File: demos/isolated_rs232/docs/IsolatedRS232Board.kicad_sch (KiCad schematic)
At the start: 9 parts, among them J1 Header1xNFemale, J2 Header1xNFemale

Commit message: export: kicad_sch — Phase 2.5b: layered placement, wire routing, KiCad 10 compatibility (#23)
* export: kicad_sch — Phase 2.5b: layered placement + routing + KiCad 9 fix

Placement (placement.py, complete rewrite):
- Replaces naive grid with Layered Signal Flow algorithm (spec §5 stages 1–8)
- Stage 1: band classification — power chips/rails at top, LEDs at bottom,
  everything else in the signal band
- Stage 2: signal-flow DAG via BFS from Rail/Connector sources; layer = BFS
  distance from nearest source
- Stage 3–4: place within (band, layer) cells at 1500-mil (38.1 mm) same-band
  spacing, 1000-mil inter-band gutter, 25.4 mm page margin
- Stage 6: cluster breakup — up to 10 iterations shifting same-band parts
  that land closer than 0.9× SAME_BAND_SPACING_MM
- Stage 8: page sized to fit (A4 → A3 → A2 → A1)
- grid_place() and sheet_size_mm() kept as shims for backward-compat

Routing (routing.py, new file):
- route_net(): connects stub ends with Manhattan L-shapes (horizontal first)
- find_junctions(): returns points where ≥3 wire endpoints coincide
- renderer uses routed wires between signal-net stub ends

Hierarchical (hierarchical.py, new file):
- collect_boards(), is_multi_board(), sub_sheet_filename() — interface stub
  for multi-Board sub-sheet emission (full implementation deferred)

KiCad 9 sub-symbol name fix (library_loader.py):
- KiCad 9 schematics expect sub-symbols nested inside their parent in
  lib_symbols to use the bare name (R_0_1, LED_0_1, 4069_1_0) — NOT the
  lib-qualified name (Device:R_0_1, Device:LED_0_1, 4xxx:4069_1_0)
- Fixed _qualify_names() to add the lib: prefix only to the exact parent
  symbol name using a lookahead (?=") that prevents sub-unit names from
  being qualified

Tests (+25 tests):
- test_placement.py: band classification, all-on-grid, determinism,
  minimum spacing, power < signal < indicator Y ordering, page sizing
- test_routing.py: H/V segments, L-shapes, orthogonality, grid snap,
  junction detection

Golden files re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
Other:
- moved on the sheet: C1, C2, C3, C4, C5, C6, C7, J1, J2

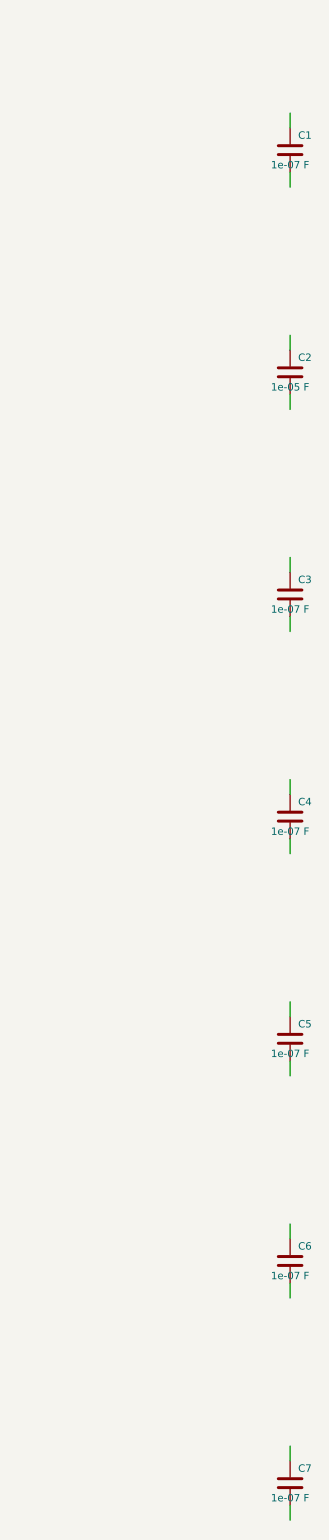
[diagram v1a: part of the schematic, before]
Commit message: framework: passive + diode terminals mandatory (#30)
Continuation of the LED.cathode regression fix (#29). Resistor,
Capacitor, Inductor, and every Diode subclass had their terminals
declared `mandatory=False` with the same "structurally inert under
graph evaluation" justification — letting demos declare BOM-only
timing / decoupling / pull-up parts without wiring them, then ship
breadboard SVGs and netlists where those parts sat orphaned.

A real resistor / capacitor / inductor / diode with a dangling
terminal does nothing. Marking the ports mandatory closes the
silent regression at the framework layer.

  - `src/components/passives/{resistor,capacitor,inductor}.py` and
    every diode subclass under `src/components/diodes/` now declare
    their terminals `mandatory=True`.
  - `tests/components/test_{resistor,capacitor,inductor}.py`:
    regression tests pin the new contract per component.
  - `tests/components/test_diode_mandatory_terminals.py` (new):
    parametrized over D1N4001 / D1N4007 / D1N4148 / D1N4728A /
    D1N4733A / D1N4742A / D1N5817.
  - Six demos (`backup_power`, `bldc_motor`, `dice`,
    `doorbell_protector`, `fan_cooling`, `isolated_rs232`) had
    declared-but-unwired passives — each now wires them either to
    their datasheet-correct net (e.g. DoorbellProtector's flyback
    diode anode joins the relay coil_minus net) or as an isolated
    0-Ω passthrough with `dynamically_driven=True` where the part
    is genuinely BOM-only and the voltage-only simulator can't
    honour its behaviour. Comments at each call site explain
    which kind.
  - Test fixtures across CLI, refdes, format-roundtrip, kicad
    import, and per-format renderer tests updated so they still
    pin down the specific error each one exists to catch without
    tripping the new mandatory-pin check first.
  - All demo docs regenerated; goldens refreshed.

After this commit the breadboard SVGs show every BOM part connected
to something — no more orphaned caps and resistors float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
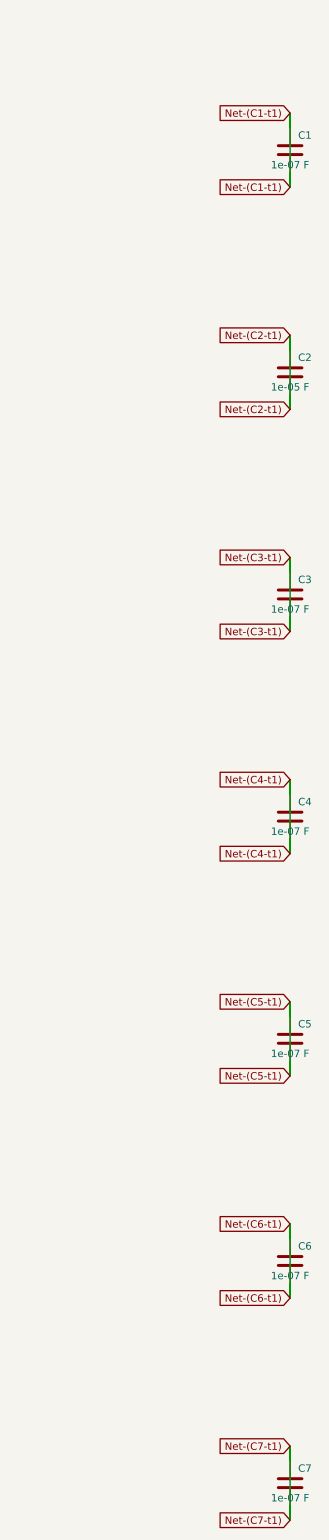
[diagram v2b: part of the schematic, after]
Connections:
- net Net-(C2-t1): now reaches C2.1
- net Net-(C2-t1): now also C2.2
- net Net-(C7-t1): now reaches C7.1
- net Net-(C7-t1): now also C7.2
- net Net-(C3-t1): now reaches C3.1
- net Net-(C3-t1): now also C3.2
- net Net-(C4-t1): now reaches C4.1
- net Net-(C4-t1): now also C4.2
- net Net-(C1-t1): now reaches C1.1
- net Net-(C1-t1): now also C1.2
- net Net-(C5-t1): now reaches C5.1
- net Net-(C5-t1): now also C5.2
- net Net-(C6-t1): now reaches C6.1
- net Net-(C6-t1): now also C6.2
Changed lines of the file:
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@@
     (stroke (width 0) (type default))
+  )
+  (global_label "Net-(C1-t1)"
+    (shape input)
+    (at 63.5 184.15 0)
+    (fields_autoplaced yes)
+    (effects (font (size 1.27 1.27)) (justify right))
+    (property "Intersheet References" "${INTERSHEET_REFS}"
+      (at 0 0 0)
+      (effects (font (size 1.27 1.27)) (hide yes))
+    )
   )
   (wire
     (pts (xy 63.5 173.99) (xy 63.5 171.45))
     (stroke (width 0) (type default))
+  )
+  (global_label "Net-(C1-t1)"
+    (shape input)
+    (at 63.5 171.45 0)
+    (fields_autoplaced yes)
+    (effects (font (size 1.27 1.27)) (justify right))
+    (property "Intersheet References" "${INTERSHEET_REFS}"
+      (at 0 0 0)
+      (effects (font (size 1.27 1.27)) (hide yes))
+    )
   )
   (symbol
@@
     (stroke (width 0) (type default))
   )
+  (global_label "Net-(C2-t1)"
+    (shape input)
+    (at 63.5 222.25 0)
+    (fields_autoplaced yes)
+    (effects (font (size 1.27 1.27)) (justify right))
+    (property "Intersheet References" "${INTERSHEET_REFS}"
+      (at 0 0 0)
+      (effects (font (size 1.27 1.27)) (hide yes))
+    )
+  )
   (wire
     (pts (xy 63.5 212.09) (xy 63.5 209.55))
     (stroke (width 0) (type default))
+  )
+  (global_label "Net-(C2-t1)"
+    (shape input)
+    (at 63.5 209.55 0)
+    (fields_autoplaced yes)
+    (effects (font (size 1.27 1.27)) (justify right))
+    (property "Intersheet References" "${INTERSHEET_REFS}"
+      (at 0 0 0)
+      (effects (font (size 1.27 1.27)) (hide yes))
+    )
   )
   (symbol
@@
     (stroke (width 0) (type default))
   )
+  (global_label "Net-(C3-t1)"
+    (shape input)
+    (at 63.5 260.35 0)
+    (fields_autoplaced yes)
+    (effects (font (size 1.27 1.27)) (justify right))
+    (property "Intersheet References" "${INTERSHEET_REFS}"
+      (at 0 0 0)
+      (effects (font (size 1.27 1.27)) (hide yes))
+    )
+  )
   (wire
     (pts (xy 63.5 250.19) (xy 63.5 247.65))
     (stroke (width 0) (type default))
+  )
+  (global_label "Net-(C3-t1)"
+    (shape input)
+    (at 63.5 247.65 0)
+    (fields_autoplaced yes)
+    (effects (font (size 1.27 1.27)) (justify right))
+    (property "Intersheet References" "${INTERSHEET_REFS}"
+      (at 0 0 0)
+      (effects (font (size 1.27 1.27)) (hide yes))
+    )
   )
   (symbol
@@
     (stroke (width 0) (type default))
   )
+  (global_label "Net-(C4-t1)"
+    (shape input)
+    (at 63.5 298.45 0)
+    (fields_autoplaced yes)
+    (effects (font (size 1.27 1.27)) (justify right))
+    (property "Intersheet References" "${INTERSHEET_REFS}"
+      (at 0 0 0)
+      (effects (font (size 1.27 1.27)) (hide yes))
+    )
+  )
   (wire
     (pts (xy 63.5 288.29) (xy 63.5 285.75))
     (stroke (width 0) (type default))
+  )
+  (global_label "Net-(C4-t1)"
+    (shape input)
+    (at 63.5 285.75 0)
+    (fields_autoplaced yes)
+    (effects (font (size 1.27 1.27)) (justify right))
+    (property "Intersheet References" "${INTERSHEET_REFS}"
+      (at 0 0 0)
+      (effects (font (size 1.27 1.27)) (hide yes))
+    )
   )
   (symbol
@@
     (stroke (width 0) (type default))
   )
+  (global_label "Net-(C5-t1)"
+    (shape input)
+    (at 63.5 336.55 0)
+    (fields_autoplaced yes)
+    (effects (font (size 1.27 1.27)) (justify right))
+    (property "Intersheet References" "${INTERSHEET_REFS}"
+      (at 0 0 0)
+      (effects (font (size 1.27 1.27)) (hide yes))
+    )
+  )
   (wire
     (pts (xy 63.5 326.39) (xy 63.5 323.85))
     (stroke (width 0) (type default))
+  )
+  (global_label "Net-(C5-t1)"
+    (shape input)
+    (at 63.5 323.85 0)
+    (fields_autoplaced yes)
+    (effects (font (size 1.27 1.27)) (justify right))
+    (property "Intersheet References" "${INTERSHEET_REFS}"
+      (at 0 0 0)
+      (effects (font (size 1.27 1.27)) (hide yes))
+    )
   )
   (symbol
@@
     (stroke (width 0) (type default))
   )
+  (global_label "Net-(C6-t1)"
+    (shape input)
+    (at 63.5 374.65 0)
+    (fields_autoplaced yes)
+    (effects (font (size 1.27 1.27)) (justify right))
+    (property "Intersheet References" "${INTERSHEET_REFS}"
+      (at 0 0 0)
+      (effects (font (size 1.27 1.27)) (hide yes))
+    )
+  )
   (wire
     (pts (xy 63.5 364.49) (xy 63.5 361.95))
     (stroke (width 0) (type default))
+  )
+  (global_label "Net-(C6-t1)"
+    (shape input)
+    (at 63.5 361.95 0)
+    (fields_autoplaced yes)
+    (effects (font (size 1.27 1.27)) (justify right))
+    (property "Intersheet References" "${INTERSHEET_REFS}"
+      (at 0 0 0)
+      (effects (font (size 1.27 1.27)) (hide yes))
+    )
   )
   (symbol
@@
     (stroke (width 0) (type default))
   )
+  (global_label "Net-(C7-t1)"
+    (shape input)
+    (at 63.5 412.75 0)
+    (fields_autoplaced yes)
+    (effects (font (size 1.27 1.27)) (justify right))
+    (property "Intersheet References" "${INTERSHEET_REFS}"
+      (at 0 0 0)
+      (effects (font (size 1.27 1.27)) (hide yes))
+    )
+  )
   (wire
     (pts (xy 63.5 402.59) (xy 63.5 400.05))
     (stroke (width 0) (type default))
+  )
+  (global_label "Net-(C7-t1)"
+    (shape input)
+    (at 63.5 400.05 0)
+    (fields_autoplaced yes)
+    (effects (font (size 1.27 1.27)) (justify right))
+    (property "Intersheet References" "${INTERSHEET_REFS}"
+      (at 0 0 0)
+      (effects (font (size 1.27 1.27)) (hide yes))
+    )
   )
   (symbol
@@
     (stroke (width 0) (type default))
   )
+  (wire
+    (pts (xy 63.5 171.45) (xy 63.5 184.15))
+    (stroke (width 0) (type default))
+  )
+  (wire
+    (pts (xy 63.5 209.55) (xy 63.5 222.25))
+    (stroke (width 0) (type default))
+  )
+  (wire
+    (pts (xy 63.5 247.65) (xy 63.5 260.35))
+    (stroke (width 0) (type default))
+  )
+  (wire
+    (pts (xy 63.5 285.75) (xy 63.5 298.45))
+    (stroke (width 0) (type default))
+  )
+  (wire
+    (pts (xy 63.5 323.85) (xy 63.5 336.55))
+    (stroke (width 0) (type default))
+  )
+  (wire
+    (pts (xy 63.5 361.95) (xy 63.5 374.65))
+    (stroke (width 0) (type default))
+  )
+  (wire
+    (pts (xy 63.5 400.05) (xy 63.5 412.75))
+    (stroke (width 0) (type default))
+  )

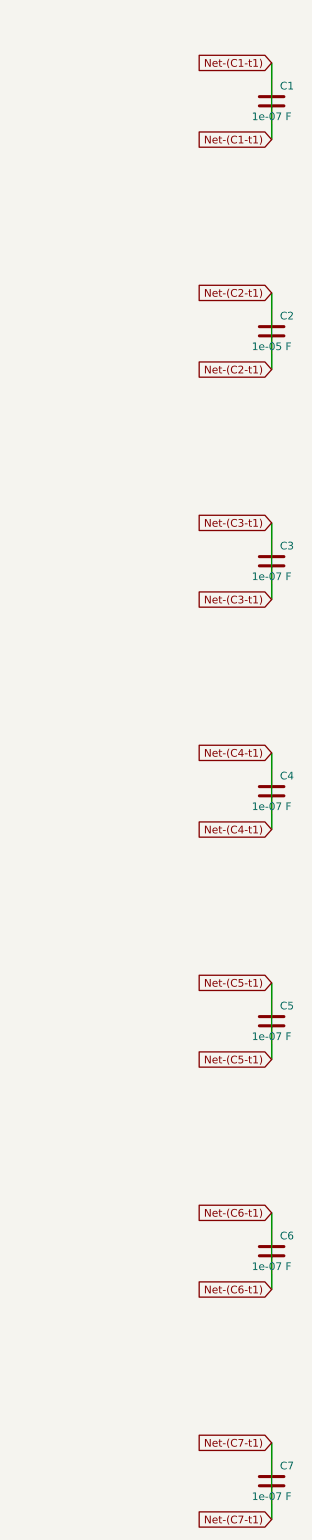
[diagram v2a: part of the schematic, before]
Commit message: units: Ohms.__str__ uses engineering notation (kΩ, MΩ, GΩ) (#33)
* units: Ohms.__str__ uses engineering notation (kΩ, MΩ, GΩ)

The previous `Ohms.__str__` formatted with bare `:.3g`, producing
unreadable scientific output for clean kilo / mega multiples:

  str(Ohms(10_000))     == "1e+04 Ω"      → now "10 kΩ"
  str(Ohms(100_000))    == "1e+05 Ω"      → now "100 kΩ"
  str(Ohms(1_000_000))  == "1e+06 Ω"      → now "1 MΩ"

The breadboard SVG visualiser surfaced the problem: a resistor body
labelled "100000Ω" makes a reader count zeros, while a label of
"100 kΩ" reads at a glance — exactly the convention every schematic
and parts catalogue uses. Centralising the engineering notation in
`Ohms.__str__` means every downstream consumer (assembly guide,
breadboard SVG, kicad netlist, BOM, reports) inherits the readable
form without each format adapter rolling its own formatter.

  - `Ohms.__str__` returns "47 Ω", "4.7 kΩ", "10 kΩ", "100 kΩ",
    "1 MΩ", "10 MΩ", "1 GΩ" per the kilo / mega / giga thresholds.
  - `Resistor.__str__` delegates to `str(self._ohms)` so it
    inherits the new notation (was producing the noisy "47.0 Ω"
    via raw float).
  - The breadboard visualiser's resistor body label uses
    `str(part.ohms)` directly (previously had a private
    `_format_ohms_compact` helper; removed).
  - `tests/components/test_resistor.py::test_str` updated for
    "47 Ω" (was "47.0 Ω"); new `test_str_renders_in_engineering_notation`
    pins kΩ / MΩ output across the kilo and mega thresholds.
  - All demo docs / goldens refreshed where the Ohms.__str__
    change affected the rendered output (breadboard SVGs, kicad
    sch value fields, BOM rows).

* units: Farads + Henries __str__ also use engineering notation

Same treatment as `Ohms.__str__` (previous commit) for the other two
passive engineering quantities. Demos contain caps and inductors
with values that the bare `:.3g` formatter would emit in scientific
form (`1e-07 F` for a 100 nF decoupling cap); centralising t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
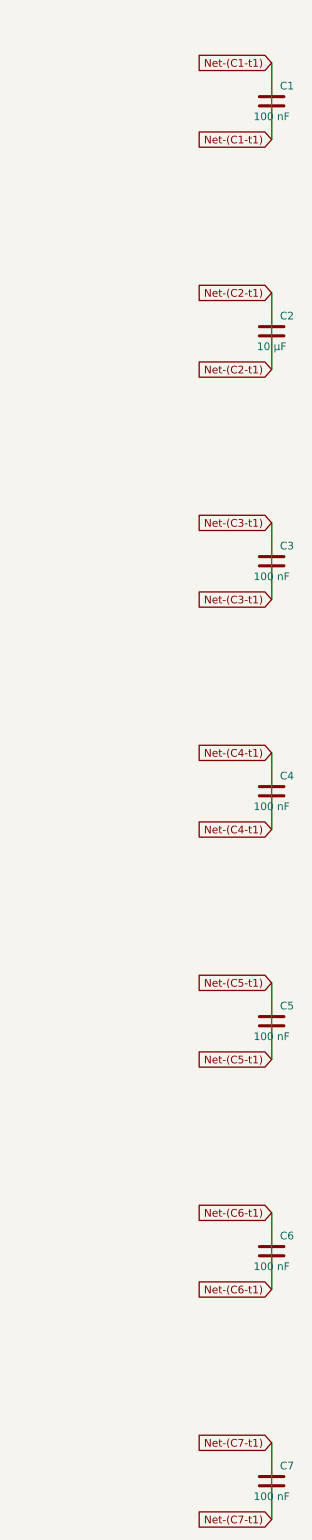
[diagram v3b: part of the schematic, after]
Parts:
- C1, C3, C4, C5, C6, C7: value 1e-07 F -> 100 nF
- C2: value 1e-05 F -> 10 µF
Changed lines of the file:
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@@
       (effects (font (size 1.27 1.27)))
     )
-    (property "Value" "1e-07 F"
+    (property "Value" "100 nF"
       (at 63.5 180.34 0)
       (effects (font (size 1.27 1.27)))
@@
       (effects (font (size 1.27 1.27)))
     )
-    (property "Value" "1e-05 F"
+    (property "Value" "10 µF"
       (at 63.5 218.44 0)
       (effects (font (size 1.27 1.27)))
@@
       (effects (font (size 1.27 1.27)))
     )
-    (property "Value" "1e-07 F"
+    (property "Value" "100 nF"
       (at 63.5 256.54 0)
       (effects (font (size 1.27 1.27)))
@@
       (effects (font (size 1.27 1.27)))
     )
-    (property "Value" "1e-07 F"
+    (property "Value" "100 nF"
       (at 63.5 294.64 0)
       (effects (font (size 1.27 1.27)))
@@
       (effects (font (size 1.27 1.27)))
     )
-    (property "Value" "1e-07 F"
+    (property "Value" "100 nF"
       (at 63.5 332.74 0)
       (effects (font (size 1.27 1.27)))
@@
       (effects (font (size 1.27 1.27)))
     )
-    (property "Value" "1e-07 F"
+    (property "Value" "100 nF"
       (at 63.5 370.84 0)
       (effects (font (size 1.27 1.27)))
@@
       (effects (font (size 1.27 1.27)))
     )
-    (property "Value" "1e-07 F"
+    (property "Value" "100 nF"
       (at 63.5 408.94 0)
       (effects (font (size 1.27 1.27)))
